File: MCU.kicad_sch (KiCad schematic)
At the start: 12 parts, among them J1 10118193-0001LF, U1 CP2102N-A01-GQFN28

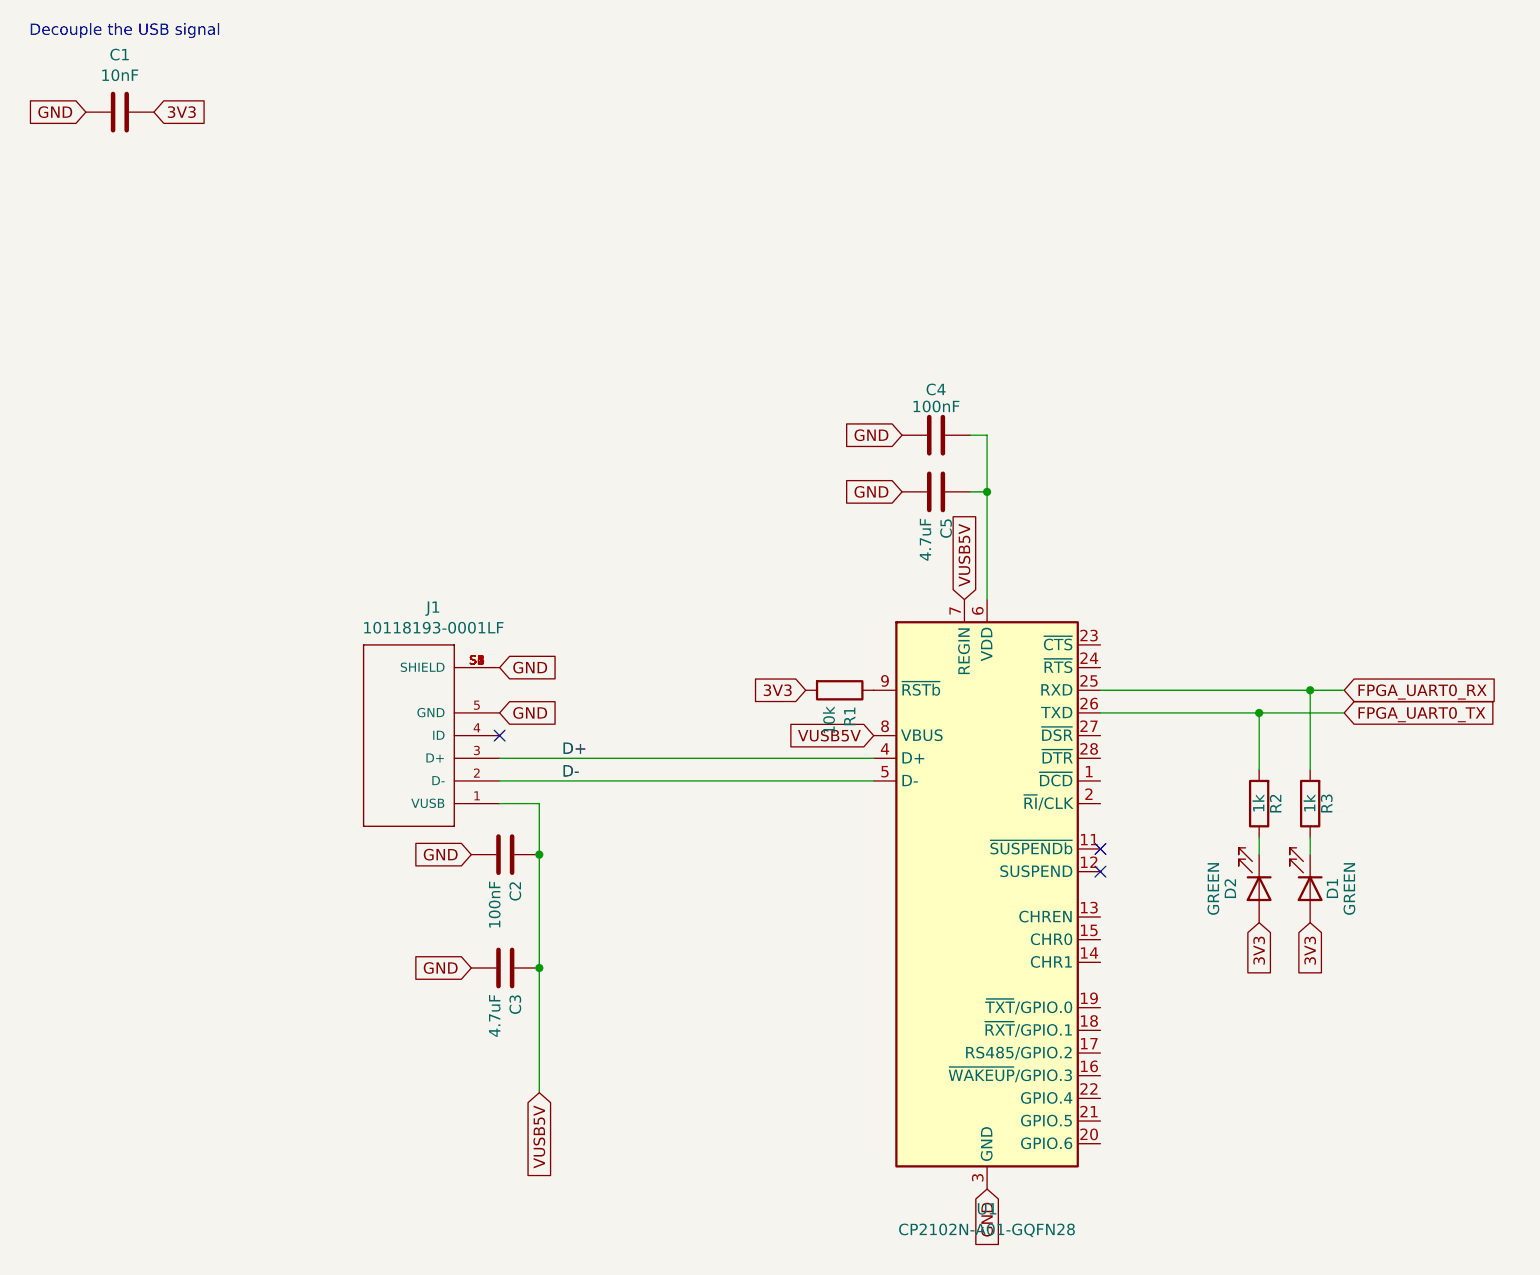
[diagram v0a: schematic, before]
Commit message: Prod version of OpenAARS 5.0 design.
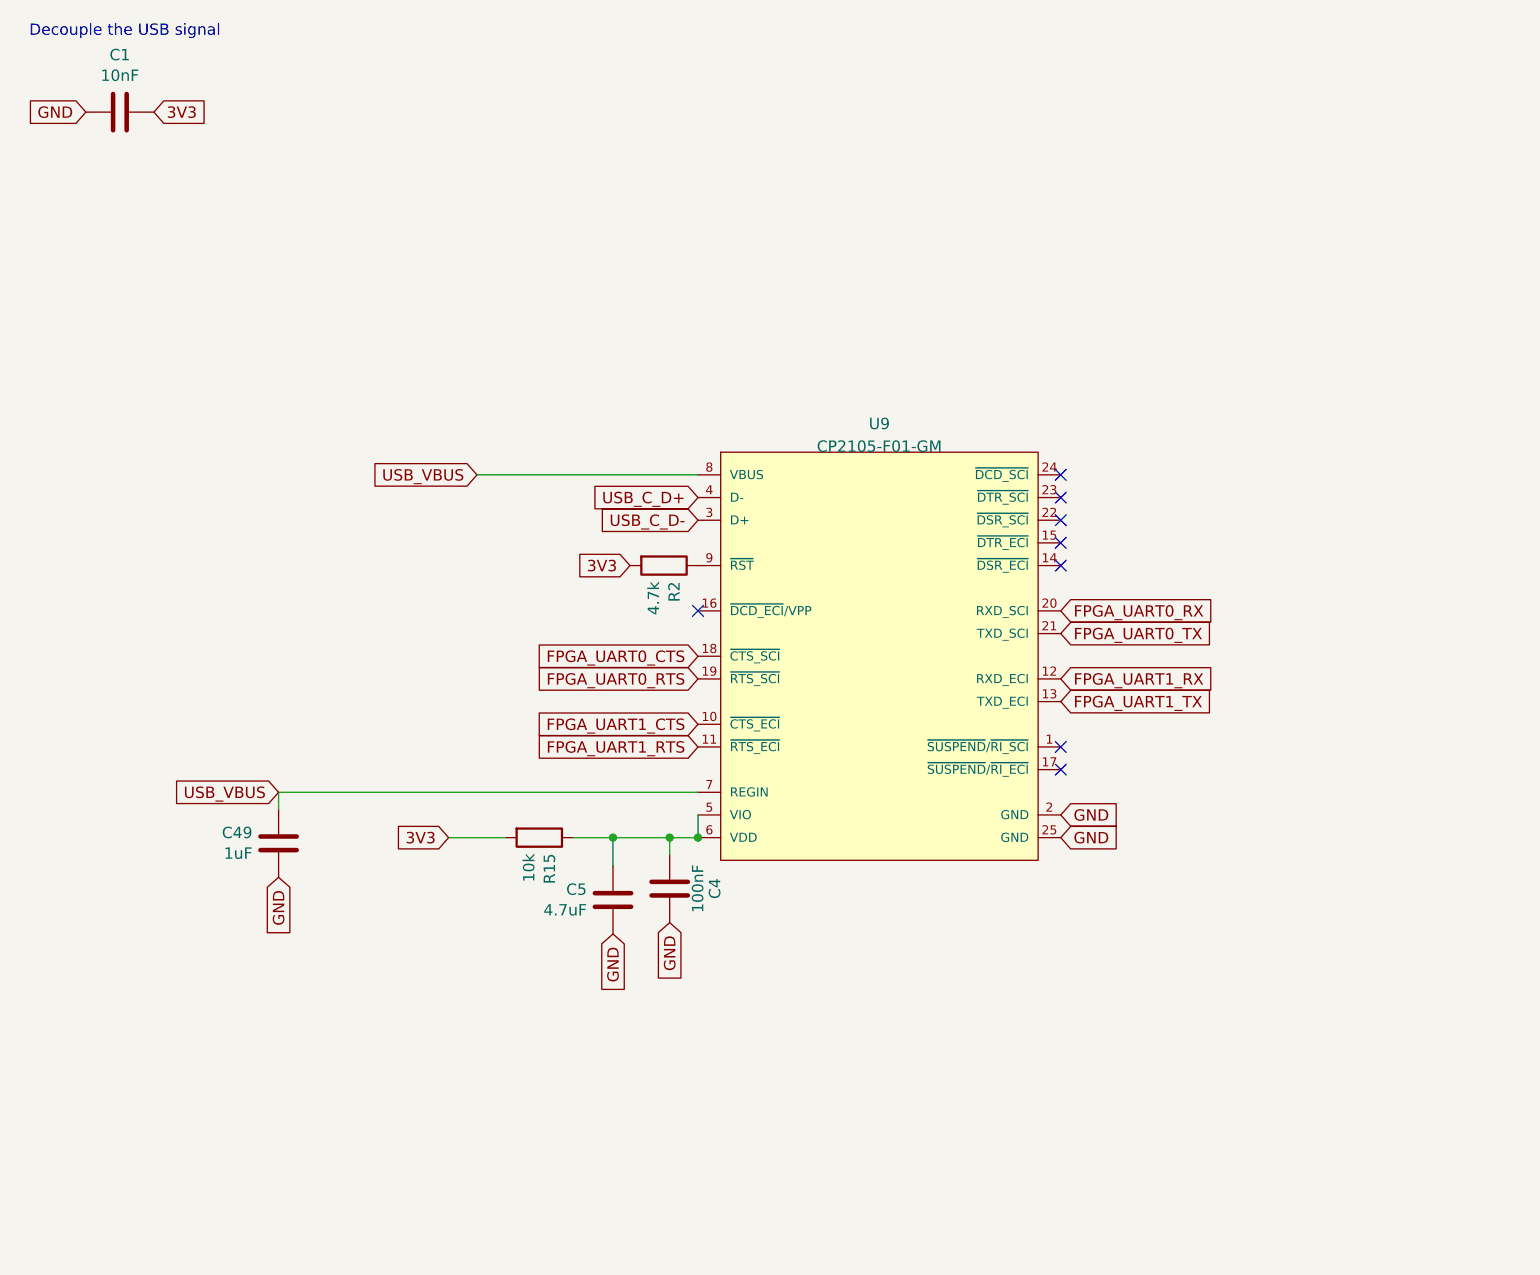
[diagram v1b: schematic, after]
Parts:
- removed C2: 100nF, Capacitor_SMD:C_0603_1608Metric, symbol Device:C
- removed C3: 4.7uF, Capacitor_SMD:C_0805_2012Metric, symbol Device:C
- removed D1, D2: GREEN, LED_SMD:LED_0603_1608Metric, symbol Device:LED
- removed J1: 10118193-0001LF, FCI_10118193-0001LF, symbol qmtech-minimig-rescue:10118193-0001LF-10118193-0001LF
- removed R1: 10k, Resistor_SMD:R_0603_1608Metric, symbol Device:R
- removed R3: 1k, Resistor_SMD:R_0603_1608Metric, symbol Device:R
- removed U1: CP2102N-A01-GQFN28, Package_DFN_QFN:QFN-28-1EP_5x5mm_P0.5mm_EP3.35x3.35mm, symbol Interface_USB:CP2102N-A01-GQFN28
- added C49: 1uF, Capacitor_SMD:C_0603_1608Metric, symbol Device:C
- added R15: 10k, Resistor_SMD:R_0603_1608Metric, symbol Device:R
- added U9: CP2105-F01-GM, KiCad-cp2105:QFN50P400X400X80-25N-D, symbol eec:CP2105-F01-GM
- R2: value 1k -> 4.7k
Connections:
- net 3V3: now also R2.2, R15.2
- net FPGA_UART0_RX: now also U9.20 (RXD_SCI)
- net FPGA_UART0_TX: now also U9.21 (TXD_SCI); no longer R2.2
- net GND: now also C49.2, U9.2 (GND), U9.25 (GND)
- net at C4.2, C5.1: now also R15.1, U9.5 (VIO), U9.6 (VDD)
- net at R2.1: now also U9.9 (~{RST})
- new net FPGA_UART0_CTS: U9.18 (~{CTS_SCI})
- new net FPGA_UART0_RTS: U9.19 (~{RTS_SCI})
- new net FPGA_UART1_CTS: U9.10 (~{CTS_ECI})
- new net FPGA_UART1_RTS: U9.11 (~{RTS_ECI})
- new net FPGA_UART1_RX: U9.12 (RXD_ECI)
- new net FPGA_UART1_TX: U9.13 (TXD_ECI)
- new net USB_C_D+: U9.4 (D-)
- new net USB_C_D-: U9.3 (D+)
- new net USB_VBUS: C49.1, U9.7 (REGIN), U9.8 (VBUS)
- no-connect marks 3 -> 8
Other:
- moved on the sheet: C4, C5
